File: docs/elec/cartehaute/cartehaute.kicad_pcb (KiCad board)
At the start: 2 copper layers, 12 parts, among them P1 Servo, P10 Analog, P11 ARU, P2 Yeux, P3 LED, P4 HUB, P5 data, P6 5V, P8 AN2, P9 AN1

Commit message: netoyage des fichiers meca, création de la base de charge
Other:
- board outline added: 38.5 x 26.5 mm
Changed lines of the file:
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@@
     (links 20)
     (no_connects 0)
-    (area 131.924999 72.924999 170.075001 93.075001)
+    (area 122.752381 69.425 187.936701 105.385)
     (thickness 1.6)
-    (drawings 0)
+    (drawings 5)
     (tracks 37)
     (zones 0)
@@
     (mod_text_size 1 1)
     (mod_text_width 0.15)
-    (pad_size 2.032 1.7272)
-    (pad_drill 1.016)
+    (pad_size 2 2)
+    (pad_drill 1.00076)
     (pad_to_mask_clearance 0.2)
-    (aux_axis_origin 132 93)
+    (aux_axis_origin 123.5 100)
     (visible_elements 7FFFFFFF)
     (pcbplotparams
       (layerselection 0x00000_80000000)
       (usegerberextensions false)
-      (excludeedgelayer true)
+      (excludeedgelayer false)
       (linewidth 0.100000)
       (plotframeref false)
@@
     (fp_line (start -2.6162 -4.1148) (end -2.1336 -5.1816) (layer Cmts.User) (width 0.381))
     (fp_line (start -2.1336 -5.1816) (end -2.1336 -3.6322) (layer Cmts.User) (width 0.381))
-    (pad 1 thru_hole circle (at -26 -15) (size 2.49936 2.49936) (drill 1.00076) (layers *.Cu *.Mask)
+    (pad 1 thru_hole circle (at -26 -15) (size 2 2) (drill 1.00076) (layers *.Cu *.Mask)
       (net 3 /GND))
     (pad 2 thru_hole circle (at -26 7.5) (size 2.49936 2.49936) (drill 1.00076) (layers *.Cu *.Mask)
@@
     (fp_line (start -2.6162 -4.1148) (end -2.1336 -5.1816) (layer Cmts.User) (width 0.381))
     (fp_line (start -2.1336 -5.1816) (end -2.1336 -3.6322) (layer Cmts.User) (width 0.381))
-    (pad 1 thru_hole circle (at 16.5 -24) (size 2.49936 2.49936) (drill 1.00076) (layers *.Cu *.Mask)
+    (pad 1 thru_hole circle (at 16.5 -24) (size 2 2) (drill 1.00076) (layers *.Cu *.Mask)
       (net 3 /GND))
     (pad 2 thru_hole circle (at 15 -1.5) (size 2.49936 2.49936) (drill 1.00076) (layers *.Cu *.Mask)
       (net 7 "Net-(P10-Pad3)"))
   )
+  (gr_line (start 123.5 100) (end 123.5 73.5) (angle 90) (layer Edge.Cuts) (width 0.15))
+  (gr_line (start 124 100) (end 123.5 100) (angle 90) (layer Edge.Cuts) (width 0.15))
+  (gr_line (start 162 100) (end 124 100) (angle 90) (layer Edge.Cuts) (width 0.15))
+  (gr_line (start 162 73.5) (end 162 100) (angle 90) (layer Edge.Cuts) (width 0.15))
+  (gr_line (start 123.5 73.5) (end 162 73.5) (angle 90) (layer Edge.Cuts) (width 0.15))
   (segment (start 125.5 81.08) (end 125.5 83.5) (width 1) (layer B.Cu) (net 1))
   (segment (start 125.5 83.5) (end 137 95) (width 1) (layer B.Cu) (net 1))
@@
     (connect_pads (clearance 0.8))
     (min_thickness 0.254)
-    (fill yes (arc_segments 16) (thermal_gap 0.5) (thermal_bridge_width 0.5))
+    (fill yes (arc_segments 16) (thermal_gap 0.8) (thermal_bridge_width 0.8))
     (polygon
       (pts
@@
     (connect_pads (clearance 0.8))
     (min_thickness 0.254)
-    (fill yes (arc_segments 16) (thermal_gap 0.5) (thermal_bridge_width 0.5))
+    (fill yes (arc_segments 16) (thermal_gap 0.8) (thermal_bridge_width 0.8))
     (polygon
       (pts

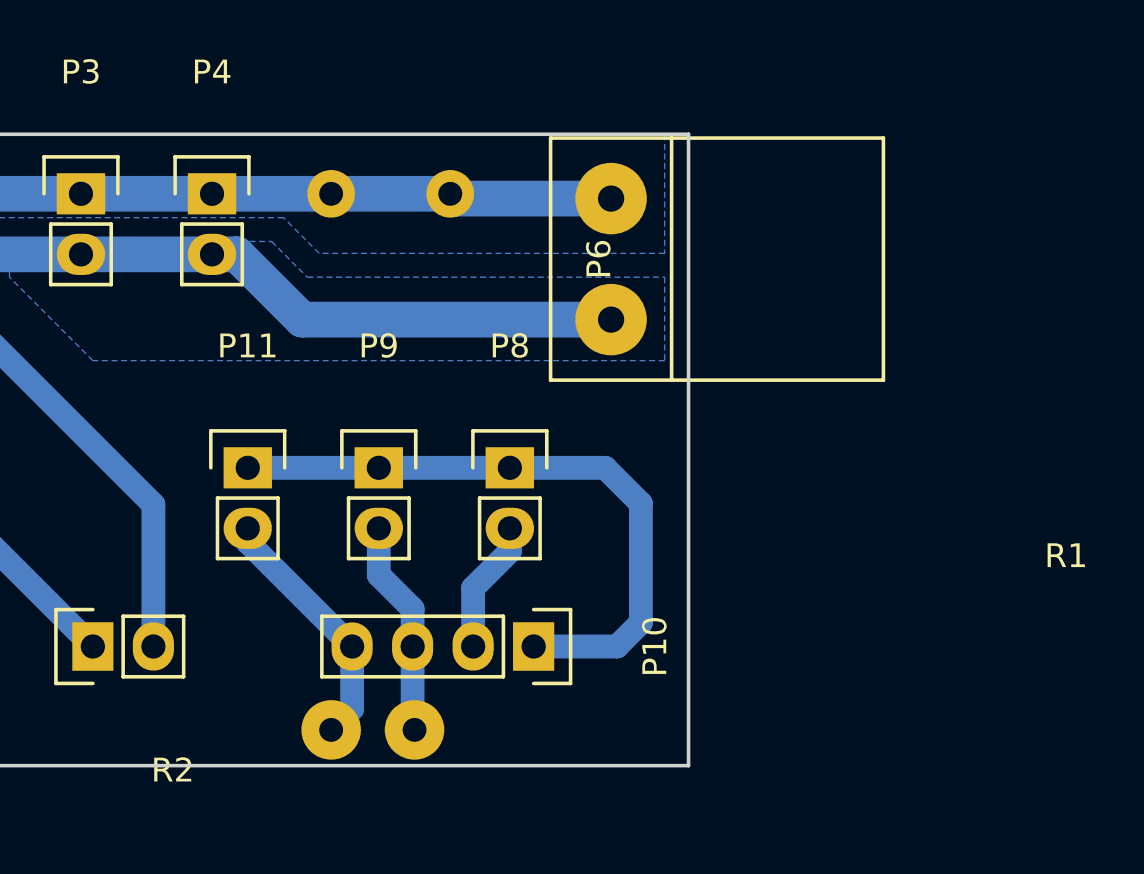
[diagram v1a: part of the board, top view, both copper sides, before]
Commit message: ajout svg elec et suppression V1
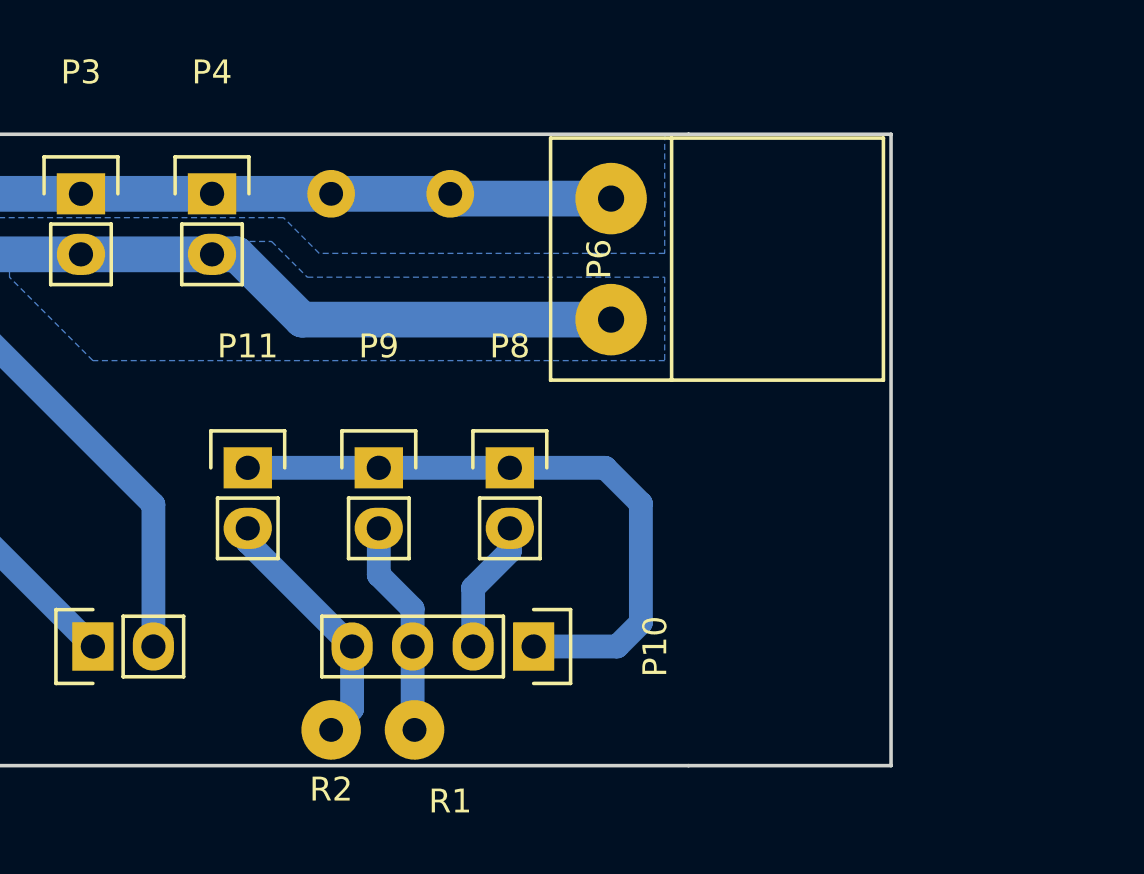
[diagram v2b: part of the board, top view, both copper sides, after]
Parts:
- P11: value ARU -> AN2
- P8: value AN2 -> ARU
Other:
- board size 38.5 x 26.5 mm -> 47 x 26.5 mm

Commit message: update elec
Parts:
- removed R1, R2: R, Wire_Connections_Bridges:WireConnection_1.00mmDrill
- added P7: data, Pin_Headers:Pin_Header_Straight_1x03_Pitch2.54mm, F.Cu at (130.7, 95.0)
- P5: value data -> Servo2; footprint Pin_Headers:Pin_Header_Straight_1x02 -> Pin_Headers:Pin_Header_Straight_1x03_Pitch2.54mm
- moved P5 25.1 mm to (120.8, 75.8), turned to 0 degrees
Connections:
- P5 pad 1: Net-(P1-Pad3) -> /GND
- P5 pad 2: Net-(P2-Pad3) -> /5V
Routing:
- net Net-(P5-Pad3): track 0.00 -> 19.6 mm
- net /GND: track 33.3 -> 38.1 mm
- net /5V: track 34.4 -> 39.2 mm
- net Net-(P10-Pad4): track 10.6 -> 6.77 mm
- net Net-(P10-Pad3): track 9.08 -> 5.55 mm
- net Net-(P1-Pad3): track 18.7 -> 17.1 mm
- net Net-(P2-Pad3): track 17.8 -> 16.5 mm
- removed copper zone on B.Cu, net /5V
- removed copper zone on B.Cu, net /GND
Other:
- board size 47 x 26.5 mm -> 51.7 x 26.5 mm

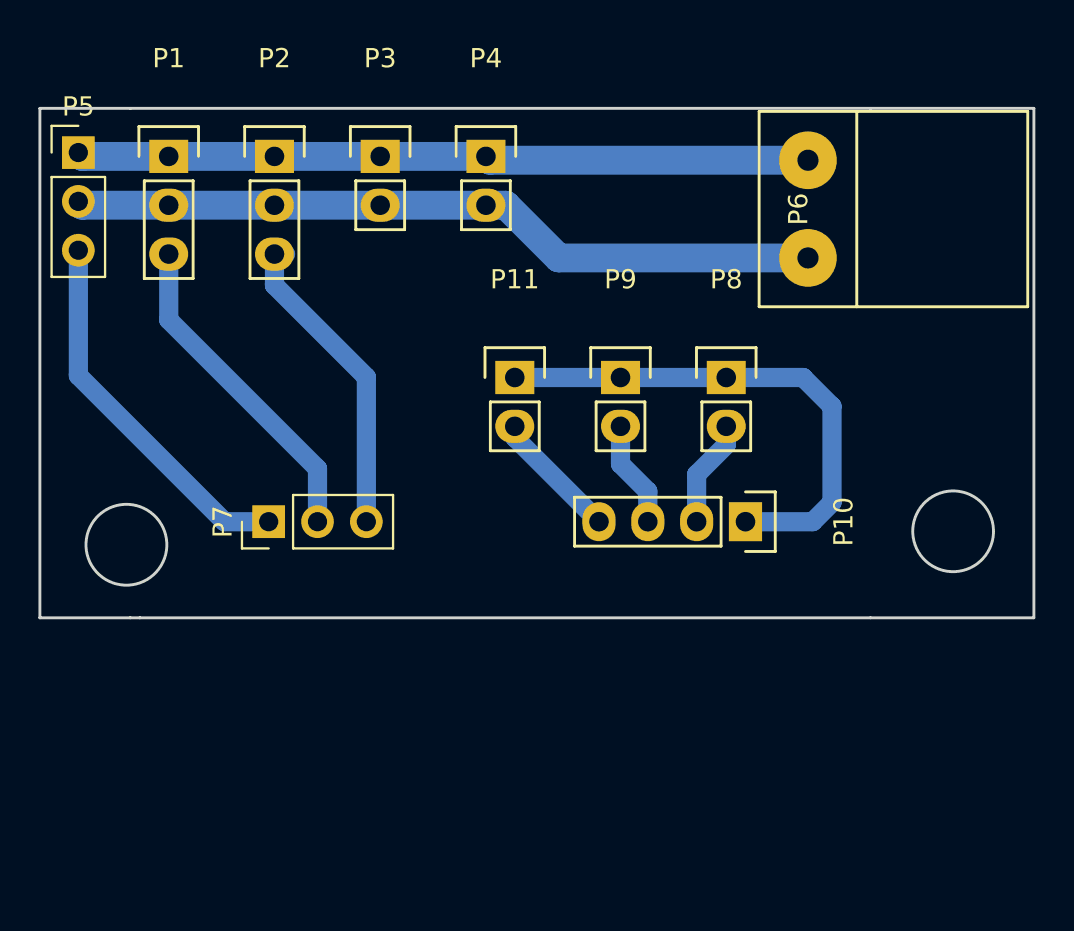
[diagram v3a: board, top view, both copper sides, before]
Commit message: Ajoute les connecteurs 12 et 19V sur la carte haute
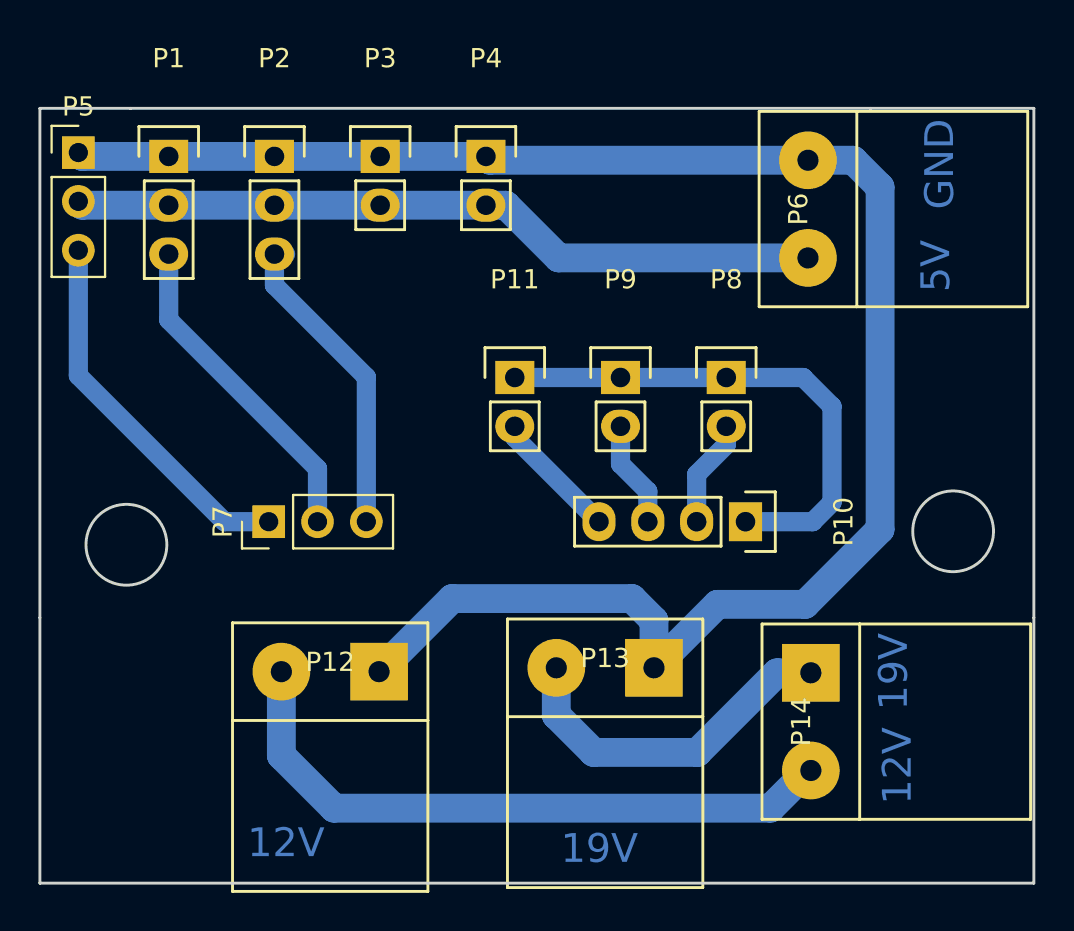
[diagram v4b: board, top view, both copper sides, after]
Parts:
- added P12: 12V, robair:Bornier5mm, F.Cu at (133.9, 102.8)
- added P13: 19V, robair:Bornier5mm, F.Cu at (148.2, 102.6)
- added P14: 19/12V, robair:Bornier5mm, F.Cu at (158.9, 105.4)
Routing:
- net /GND: track 38.1 -> 93.8 mm
- net Net-(P12-Pad2): track 0.00 -> 33.8 mm
- net Net-(P13-Pad2): track 0.00 -> 18.2 mm
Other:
- board size 51.7 x 26.5 mm -> 51.7 x 40.3 mm
- board text added: "12V"
- board text added: "19V"
- board text added: "5V"
- board text added: "GND"
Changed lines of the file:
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@@
 (kicad_pcb (version 4) (host pcbnew 4.0.4-stable)
   (general
-    (links 19)
+    (links 23)
     (no_connects 0)
-    (area 123.424999 73.424999 170.575001 100.075001)
+    (area 117.57619 69.425 171.105001 115.005001)
     (thickness 1.6)
-    (drawings 11)
-    (tracks 40)
+    (drawings 16)
+    (tracks 60)
     (zones 0)
-    (modules 11)
-    (nets 10)
+    (modules 14)
+    (nets 12)
   )
   (page A4)
@@
   (net 8 "Net-(P10-Pad4)")
   (net 9 "Net-(P5-Pad3)")
+  (net 10 "Net-(P12-Pad2)")
+  (net 11 "Net-(P13-Pad2)")
   (net_class Default "Ceci est la Netclass par défaut"
     (clearance 0.7)
@@
     (add_net /5V)
     (add_net /GND)
+    (add_net "Net-(P12-Pad2)")
+    (add_net "Net-(P13-Pad2)")
   )
   (module Pin_Headers:Pin_Header_Straight_1x02 (layer F.Cu)
@@
     )
   )
+  (module robair:Bornier5mm (layer F.Cu)
+    (at 133.9 102.8 180)
+    (fp_text reference P12 (at 0 0.5 180) (layer F.SilkS)
+      (effects (font (size 1 1) (thickness 0.15)))
+    )
+    (fp_text value 12V (at 0 -0.5 180) (layer F.Fab)
+      (effects (font (size 1 1) (thickness 0.15)))
+    )
+    (fp_line (start -5.08 -11.43) (end 5.08 -11.43) (layer F.SilkS) (width 0.15))
+    (fp_line (start 5.08 -11.43) (end 5.08 -2.54) (layer F.SilkS) (width 0.15))
+    (fp_line (start -5.08 -11.43) (end -5.08 -2.54) (layer F.SilkS) (width 0.15))
+    (fp_line (start -5.08 -2.54) (end -5.08 2.54) (layer F.SilkS) (width 0.15))
+    (fp_line (start -5.08 2.54) (end 5.08 2.54) (layer F.SilkS) (width 0.15))
+    (fp_line (start 5.08 2.54) (end 5.08 -2.54) (layer F.SilkS) (width 0.15))
+    (fp_line (start 5.08 -2.54) (end -5.08 -2.54) (layer F.SilkS) (width 0.15))
+    (pad 1 thru_hole rect (at -2.54 0 180) (size 3 3) (drill 1.1) (layers *.Cu *.Mask)
+      (net 3 /GND))
+    (pad 2 thru_hole circle (at 2.54 0 180) (size 3 3) (drill 1.1) (layers *.Cu *.Mask)
+      (net 10 "Net-(P12-Pad2)"))
+  )
+  (module robair:Bornier5mm (layer F.Cu)
+    (at 148.2 102.6 180)
+    (fp_text reference P13 (at 0 0.5 180) (layer F.SilkS)
+      (effects (font (size 1 1) (thickness 0.15)))
+    )
+    (fp_text value 19V (at 0 -0.5 180) (layer F.Fab)
+      (effects (font (size 1 1) (thickness 0.15)))
+    )
+    (fp_line (start -5.08 -11.43) (end 5.08 -11.43) (layer F.SilkS) (width 0.15))
+    (fp_line (start 5.08 -11.43) (end 5.08 -2.54) (layer F.SilkS) (width 0.15))
+    (fp_line (start -5.08 -11.43) (end -5.08 -2.54) (layer F.SilkS) (width 0.15))
+    (fp_line (start -5.08 -2.54) (end -5.08 2.54) (layer F.SilkS) (width 0.15))
+    (fp_line (start -5.08 2.54) (end 5.08 2.54) (layer F.SilkS) (width 0.15))
+    (fp_line (start 5.08 2.54) (end 5.08 -2.54) (layer F.SilkS) (width 0.15))
+    (fp_line (start 5.08 -2.54) (end -5.08 -2.54) (layer F.SilkS) (width 0.15))
+    (pad 1 thru_hole rect (at -2.54 0 180) (size 3 3) (drill 1.1) (layers *.Cu *.Mask)
+      (net 3 /GND))
+    (pad 2 thru_hole circle (at 2.54 0 180) (size 3 3) (drill 1.1) (layers *.Cu *.Mask)
+      (net 11 "Net-(P13-Pad2)"))
+  )
+  (module robair:Bornier5mm (layer F.Cu)
+    (at 158.9 105.4 270)
+    (fp_text reference P14 (at 0 0.5 270) (layer F.SilkS)
+      (effects (font (size 1 1) (thickness 0.15)))
+    )
+    (fp_text value 19/12V (at 0 -0.5 270) (layer F.Fab)
+      (effects (font (size 1 1) (thickness 0.15)))
+    )
+    (fp_line (start -5.08 -11.43) (end 5.08 -11.43) (layer F.SilkS) (width 0.15))
+    (fp_line (start 5.08 -11.43) (end 5.08 -2.54) (layer F.SilkS) (width 0.15))
+    (fp_line (start -5.08 -11.43) (end -5.08 -2.54) (layer F.SilkS) (width 0.15))
+    (fp_line (start -5.08 -2.54) (end -5.08 2.54) (layer F.SilkS) (width 0.15))
+    (fp_line (start -5.08 2.54) (end 5.08 2.54) (layer F.SilkS) (width 0.15))
+    (fp_line (start 5.08 2.54) (end 5.08 -2.54) (layer F.SilkS) (width 0.15))
+    (fp_line (start 5.08 -2.54) (end -5.08 -2.54) (layer F.SilkS) (width 0.15))
+    (pad 1 thru_hole rect (at -2.54 0 270) (size 3 3) (drill 1.1) (layers *.Cu *.Mask)
+      (net 11 "Net-(P13-Pad2)"))
+    (pad 2 thru_hole circle (at 2.54 0 270) (size 3 3) (drill 1.1) (layers *.Cu *.Mask)
+      (net 10 "Net-(P12-Pad2)"))
+  )
+  (gr_text 19V (at 147.9 112) (layer B.Cu)
+    (effects (font (size 1.5 1.5) (thickness 0.3)))
+  )
+  (gr_text 12V (at 131.6 111.7) (layer B.Cu)
+    (effects (font (size 1.5 1.5) (thickness 0.3)))
+  )
+  (gr_text 19V (at 163.2 102.8 90) (layer B.Cu)
+    (effects (font (size 1.5 1.5) (thickness 0.3)))
+  )
+  (gr_text 12V (at 163.4 107.7 90) (layer B.Cu)
+    (effects (font (size 1.5 1.5) (thickness 0.3)))
+  )
+  (gr_text 5V (at 165.4 81.7 90) (layer B.Cu)
+    (effects (font (size 1.5 1.5) (thickness 0.3)))
+  )
+  (gr_text GND (at 165.6 76.4 90) (layer B.Cu)
+    (effects (font (size 1.5 1.5) (thickness 0.3)))
+  )
+  (gr_line (start 118.8 113.8) (end 118.8 100) (angle 90) (layer Edge.Cuts) (width 0.15))
+  (gr_line (start 170.5 113.8) (end 118.8 113.8) (angle 90) (layer Edge.Cuts) (width 0.15))
+  (gr_line (start 170.5 100) (end 170.5 113.8) (angle 90) (layer Edge.Cuts) (width 0.15))
   (gr_circle (center 166.3 95.5) (end 164.2 95.5) (layer Edge.Cuts) (width 0.15))
   (gr_circle (center 123.3 96.2) (end 121.2 96.1) (layer Edge.Cuts) (width 0.15))
-  (gr_line (start 118.8 100) (end 123.5 100) (angle 90) (layer Edge.Cuts) (width 0.15))
   (gr_line (start 118.8 73.5) (end 118.8 100) (angle 90) (layer Edge.Cuts) (width 0.15))
   (gr_line (start 123.5 73.5) (end 118.8 73.5) (angle 90) (layer Edge.Cuts) (width 0.15))
-  (gr_line (start 170.5 100) (end 162 100) (angle 90) (layer Edge.Cuts) (width 0.15))
   (gr_line (start 170.5 73.5) (end 170.5 100) (angle 90) (layer Edge.Cuts) (width 0.15))
   (gr_line (start 162 73.5) (end 170.5 73.5) (angle 90) (layer Edge.Cuts) (width 0.15))
-  (gr_line (start 124 100) (end 123.5 100) (angle 90) (layer Edge.Cuts) (width 0.15))
-  (gr_line (start 162 100) (end 124 100) (angle 90) (layer Edge.Cuts) (width 0.15))
   (gr_line (start 123.5 73.5) (end 162 73.5) (angle 90) (layer Edge.Cuts) (width 0.15))
   (segment (start 133.24 95) (end 133.24 92.24) (width 1) (layer B.Cu) (net 1))
@@
   (segment (start 131 82.7) (end 135.78 87.48) (width 1) (layer B.Cu) (net 2))
   (segment (start 131 81.08) (end 131.58 81.08) (width 1) (layer B.Cu) (net 2))
-  (segment (start 158.75 76.2) (end 142.2 76.2) (width 1.5) (layer B.Cu) (net 3) (status C00000))
-  (segment (start 142.2 76.2) (end 142 76) (width 1.5) (layer B.Cu) (net 3) (status C00000))
+  (segment (start 150.74 102.6) (end 150.74 100.14) (width 1.5) (layer B.Cu) (net 3))
+  (segment (start 140.24 99) (end 136.44 102.8) (width 1.5) (layer B.Cu) (net 3))
+  (segment (start 149.6 99) (end 140.24 99) (width 1.5) (layer B.Cu) (net 3))
+  (segment (start 150.74 100.14) (end 149.6 99) (width 1.5) (layer B.Cu) (net 3))
+  (segment (start 158.75 76.2) (end 161.1 76.2) (width 1.5) (layer B.Cu) (net 3))
+  (segment (start 154.04 99.3) (end 150.74 102.6) (width 1.5) (layer B.Cu) (net 3))
+  (segment (start 158.6 99.3) (end 154.04 99.3) (width 1.5) (layer B.Cu) (net 3))
+  (segment (start 162.5 95.4) (end 158.6 99.3) (width 1.5) (layer B.Cu) (net 3))
+  (segment (start 162.5 77.6) (end 162.5 95.4) (width 1.5) (layer B.Cu) (net 3))
+  (segment (start 161.1 76.2) (end 162.5 77.6) (width 1.5) (layer B.Cu) (net 3))
+  (segment (start 158.75 76.2) (end 142.2 76.2) (width 1.5) (layer B.Cu) (net 3))
+  (segment (start 142.2 76.2) (end 142 76) (width 1.5) (layer B.Cu) (net 3))
   (segment (start 125.5 76) (end 121 76) (width 1.5) (layer B.Cu) (net 3))
   (segment (start 121 76) (end 120.8 75.8) (width 1.5) (layer B.Cu) (net 3))
@@
   (segment (start 120.8 87.4) (end 120.8 80.88) (width 1) (layer B.Cu) (net 9))
   (segment (start 128.4 95) (end 120.8 87.4) (width 1) (layer B.Cu) (net 9))
+  (segment (start 158.9 107.94) (end 158.76 107.94) (width 1) (layer B.Cu) (net 10))
+  (segment (start 158.76 107.94) (end 156.8 109.9) (width 1.5) (layer B.Cu) (net 10))
+  (segment (start 156.8 109.9) (end 134.1 109.9) (width 1.5) (layer B.Cu) (net 10))
+  (segment (start 134.1 109.9) (end 131.36 107.16) (width 1.5) (layer B.Cu) (net 10))
+  (segment (start 131.36 107.16) (end 131.36 102.8) (width 1.5) (layer B.Cu) (net 10))
+  (segment (start 158.9 102.86) (end 157.14 102.86) (width 1.5) (layer B.Cu) (net 11))
+  (segment (start 145.66 105.06) (end 145.66 102.6) (width 1.5) (layer B.Cu) (net 11))
+  (segment (start 147.6 107) (end 145.66 105.06) (width 1.5) (layer B.Cu) (net 11))
+  (segment (start 153 107) (end 147.6 107) (width 1.5) (layer B.Cu) (net 11))
+  (segment (start 157.14 102.86) (end 153 107) (width 1.5) (layer B.Cu) (net 11))
 )
